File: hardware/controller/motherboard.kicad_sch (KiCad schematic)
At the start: 55 parts, among them J10 TC2030, J2 Molex PicoBlade, J3 Conn_02x03_Counter_Clockwise, J4 AFB10-S18LCA-00, J5 726386-2, J6 Conn_Coaxial_Small, J7 AFB10-S06LCA-00, J9 PinHeader 1x10 P1.00mm, Q1 AO3401A, SW1 SW_Push, U1 nRF52840-QIAA, U2 nPM1300-QEAA, Y1 32MHz, Y2 32.768 kHz

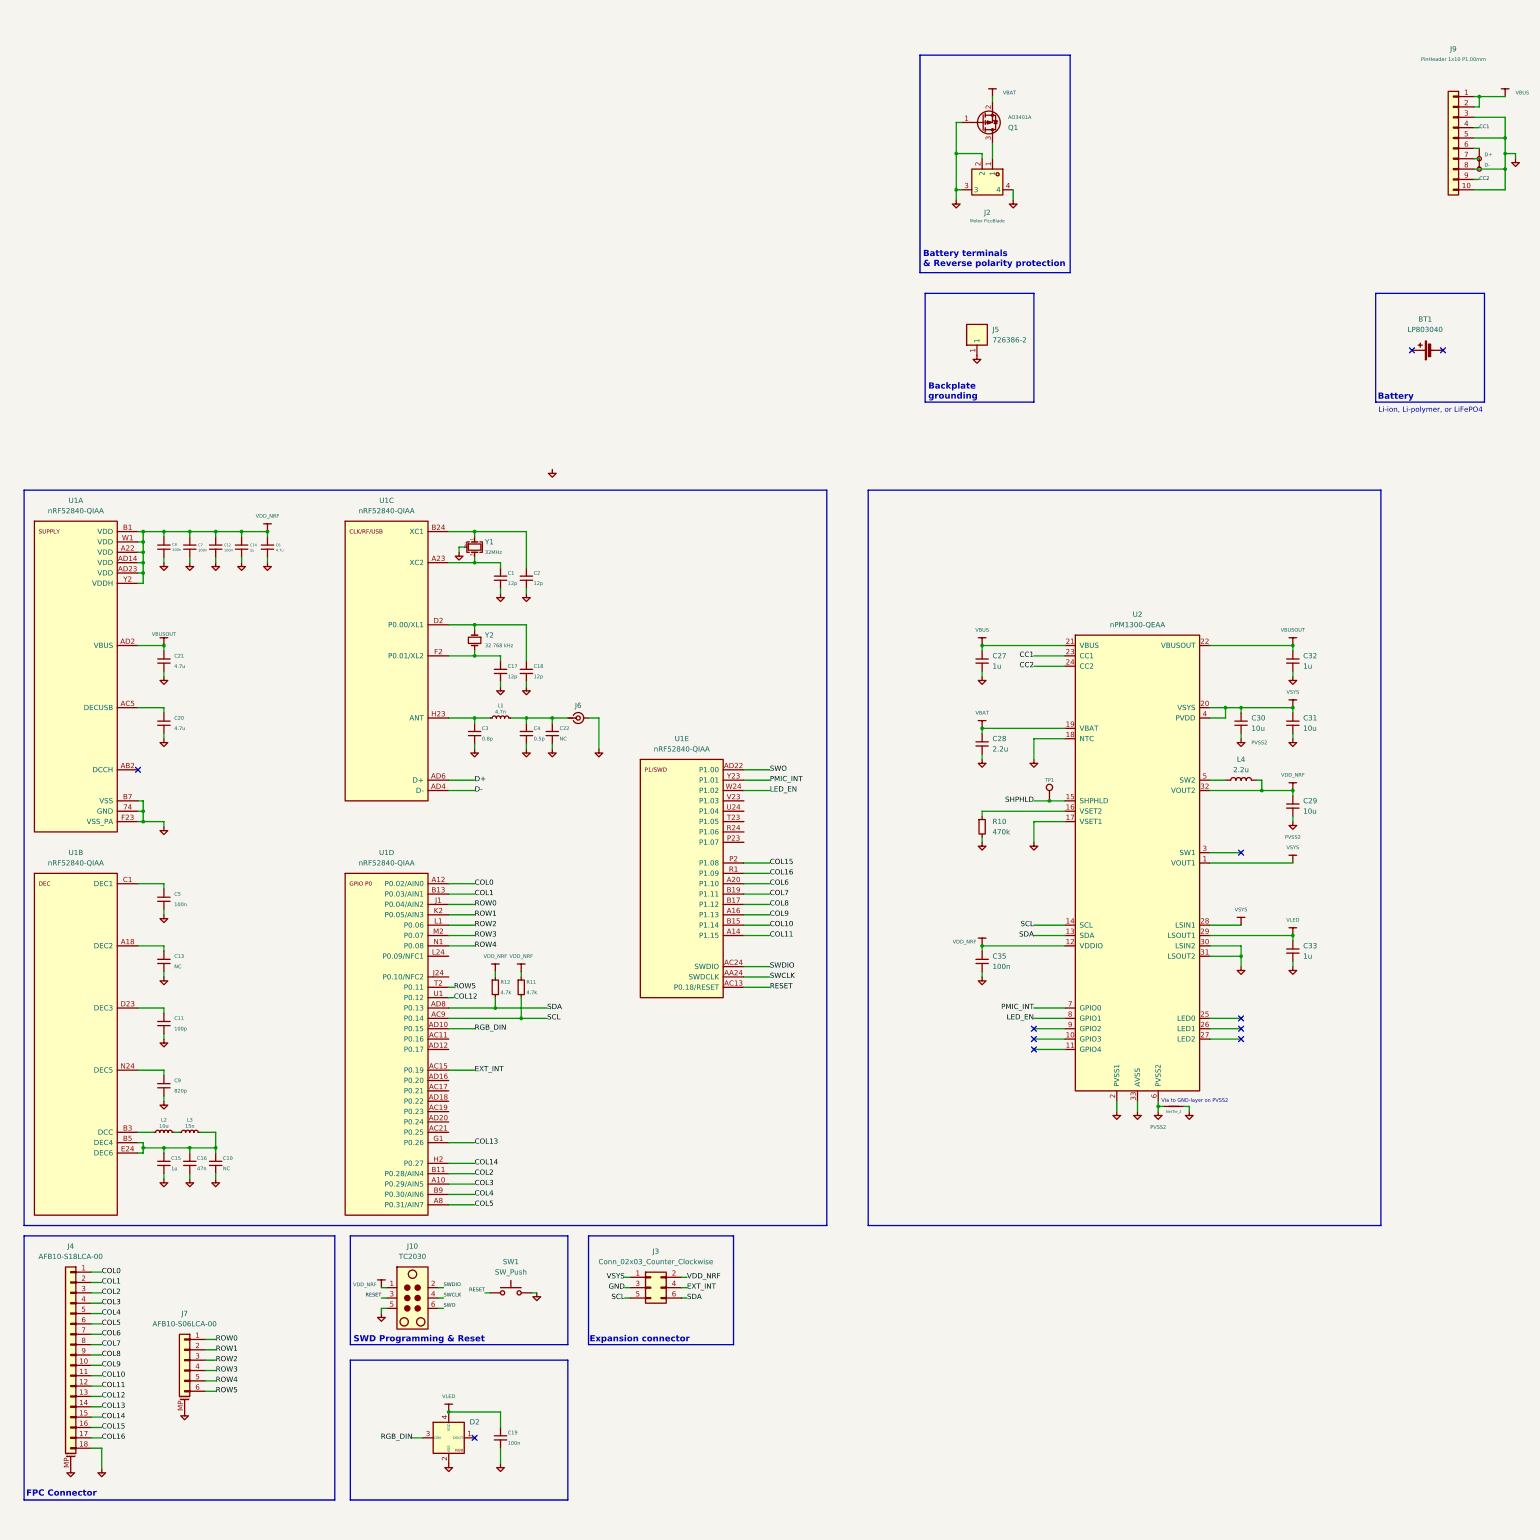
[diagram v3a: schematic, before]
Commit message: feat(controller): MB cleanup before ERC, Q1 PMPB15XP, Y1 NX2016SA, MB-DB pinout (A12, P9, M1, I6)
- no-connects on unused nRF52840 and nPM1300 pins; C10, C13, BT1 removed;
  C22 DNP; PVSS2 drawn with new easyeda2kicad:pgnd; J5 as Conn_01x01;
  J2 as Conn_01x02_MountingPin
- Q1: Nexperia PMPB15XP,115 (C513107), new ibm_m:PMPB15XP symbol,
  DFN2020MD-6 footprint and 3D model imported via easyeda2kicad
- Y1: NDK NX2016SA-32MHZ-EXS00A-CS06654 (C5441424), CL 8 pF
- J8/J9 pinout: VBUS, VBUS, CC1, GND, D+, D-, GND, CC2, GND, GND
- easyeda2kicad.kicad_sym: remove premature closing paren that hid 10 symbols
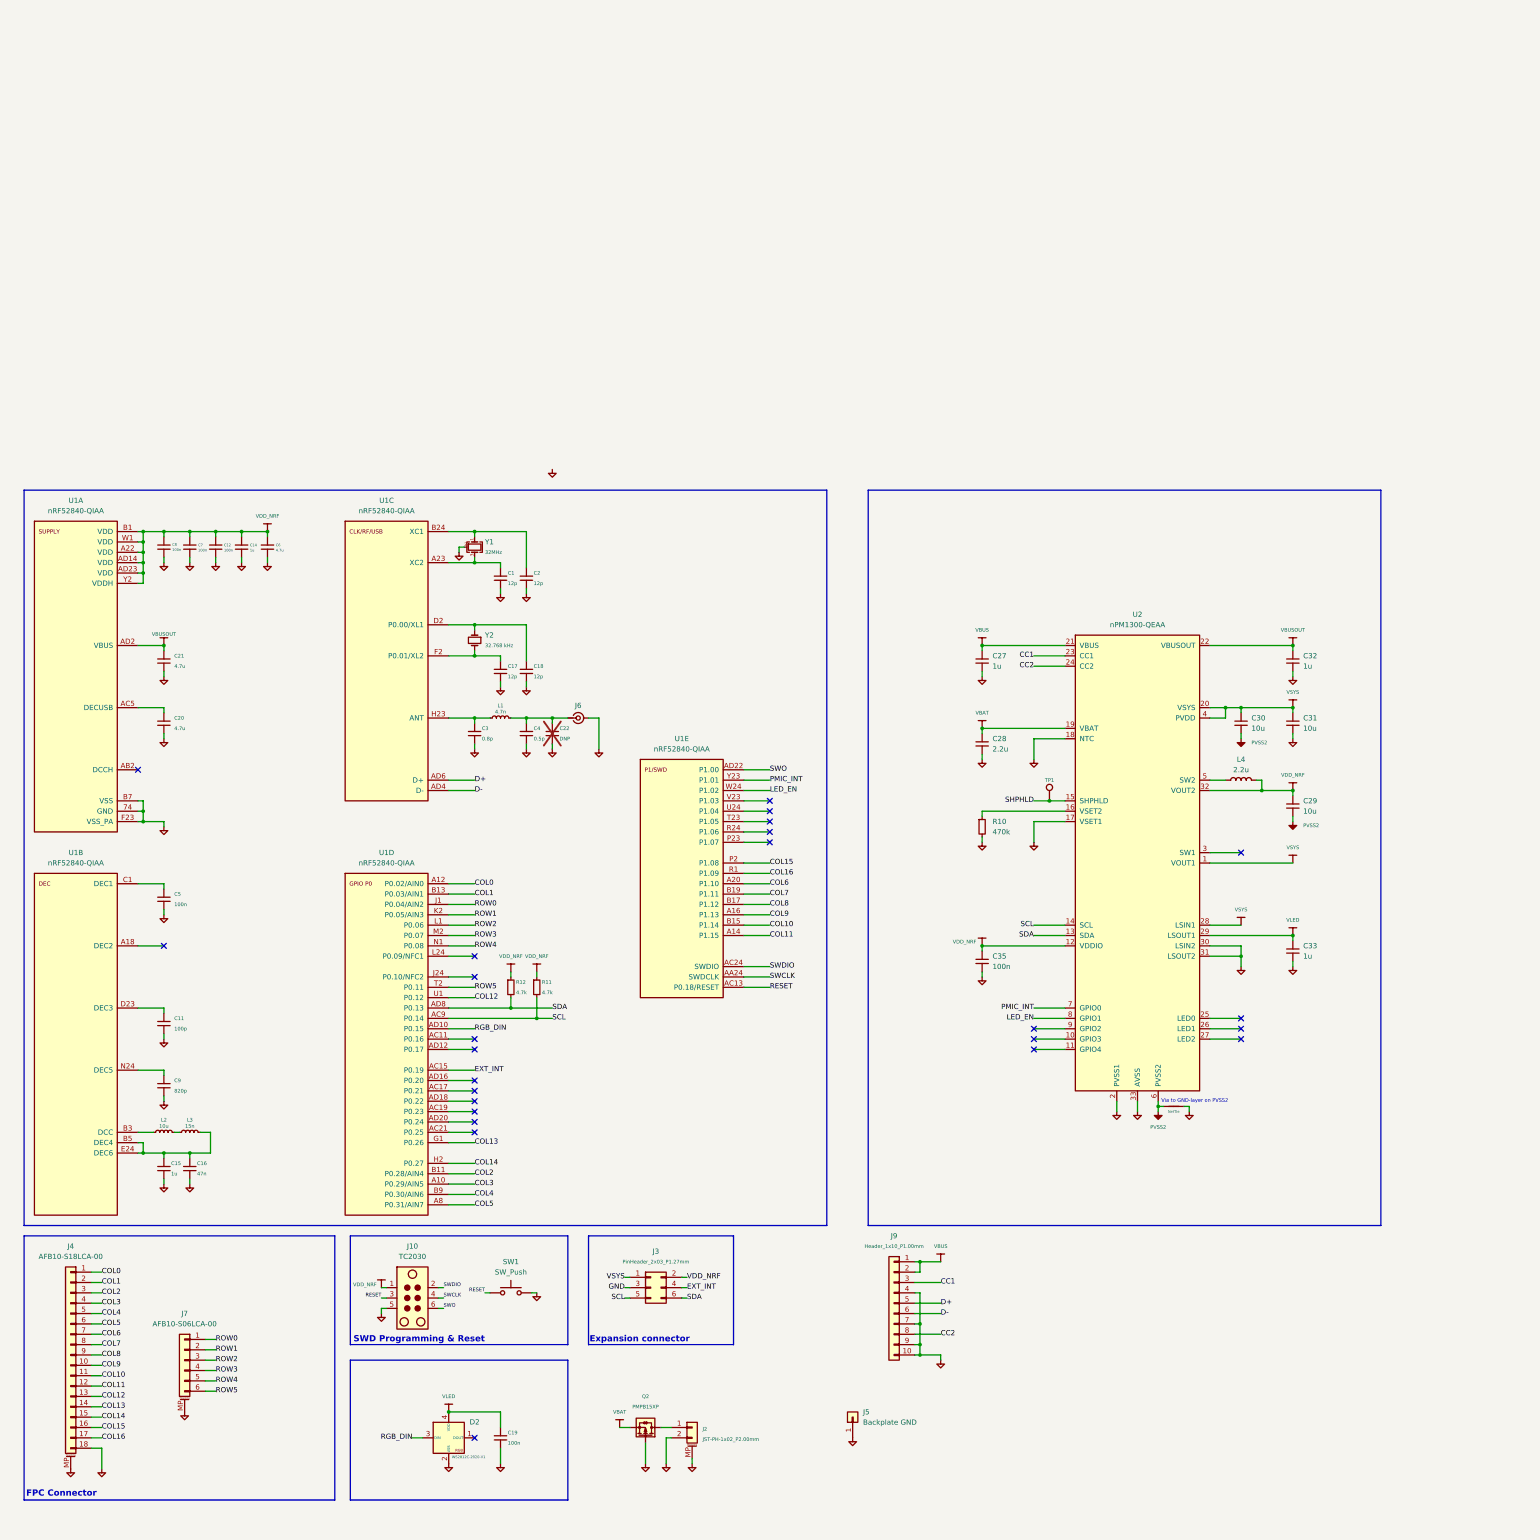
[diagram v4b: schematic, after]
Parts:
- removed BT1: LP803040, easyeda2kicad:LP803040, symbol Device:Battery_Cell
- removed C10, C13: NC, Capacitor_SMD:C_0402_1005Metric, symbol Device:C_Small
- removed J2: Molex PicoBlade, easyeda2kicad:CONN-SMD_P2.00_S2B-PH-SM4-TB-LF-SN, symbol easyeda2kicad:S2B-PH-SM4-TB(LF)(SN)
- removed Q1: AO3401A, Package_TO_SOT_SMD:SOT-23, symbol Transistor_FET:AO3401A
- added J2: JST-PH-1x02_P2.00mm, Connector_JST:JST_PH_S2B-PH-SM4-TB_1x02-1MP_P2.00mm_Horizontal, symbol Connector_Generic_MountingPin:Conn_01x02_MountingPin
- added Q2: PMPB15XP, easyeda2kicad:DFN2020MD-6_L2.0-W2.0-P0.65-BL, symbol ibm_m:PMPB15XP
- C22: value NC -> DNP; now not fitted
- D2: value rgb -> WS2812C-2020-V1
- J3: value Conn_02x03_Counter_Clockwise -> PinHeader_2x03_P1.27mm
- J5: value 726386-2 -> Backplate GND; symbol easyeda2kicad:726386-2 -> Connector_Generic:Conn_01x01
- J9: value PinHeader 1x10 P1.00mm -> Header_1x10_P1.00mm
- NT1: value NetTie_2 -> NetTie
- Y1: LCSC Part C255896 -> C5441424
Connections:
- net CC1: now also J9.3 (Pin_3); no longer J9.4 (Pin_4)
- net CC2: now also J9.8 (Pin_8); no longer J9.9 (Pin_9)
- net D+: now also J9.5 (Pin_5); no longer J9.6 (Pin_6)
- net D-: now also J9.6 (Pin_6); no longer J9.7 (Pin_7)
- net GND: now also J9.4 (Pin_4), J9.7 (Pin_7), J9.9 (Pin_9), J2.2 (Pin_2), J2.MP (MountPin), Q2.3 (G); no longer J9.3 (Pin_3), J9.5 (Pin_5), J9.8 (Pin_8)
- net VBAT: now also Q2.4 (S), Q2.8 (S)
- new net: J2.1 (Pin_1), Q2.1 (D), Q2.2 (D), Q2.5 (D), Q2.6 (D), Q2.7 (D)
- no-connect marks 11 -> 25
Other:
- note removed: "Backplate grounding"
- note removed: "Battery"
- note removed: "Battery terminals & Reverse polarity protection"
- note removed: "Li-ion, Li-polymer, or LiFePO4"
- moved on the sheet: C15, C16, J5, J9, R11, R12

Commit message: feat(controller): VBUS protection F1/D1, TPD4E05U06 symbol, ERC power flags (I3)
- F1 SMD1210-110-24V (C22436715), D1 SMF20A (C123788) as D_Zener_Small, cathode on DB_VBUS
- U3 on new ibm_m:TPD4E05U06DQA symbol, connections unchanged
- ERC sheet with PWR_FLAG for VBUS, VBAT, PVSS2, DB_VBUS, DB_GND
- C19 footprint 0402
- docs: I3 applied, J2 = JST PH, WS2812C VIH resolved
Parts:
- C19: footprint Package_SON:WSON-8-1EP_6x5mm_P1.27mm_EP3.4x4mm -> Capacitor_SMD:C_0402_1005Metric
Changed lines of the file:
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@@
 			)
 		)
-		(property "Footprint" "Package_SON:WSON-8-1EP_6x5mm_P1.27mm_EP3.4x4mm"
+		(property "Footprint" "Capacitor_SMD:C_0402_1005Metric"
 			(at 165.1 247.65 0)
 			(hide yes)
